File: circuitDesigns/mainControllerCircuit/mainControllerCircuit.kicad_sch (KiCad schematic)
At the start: 49 parts, among them J1 USB_A, J2 USB_A, J3 USB_A, J4 Conn_01x15_Pin, J5 Conn_01x15_Pin, J6 Conn_01x16_Socket, J7 OutputVCC, Q1 AO3400A, Q10 AO3400A, Q11 AO3400A, Q12 AO3400A, Q13 AO3400A, Q14 AO3400A, Q15 AO3400A, Q16 AO3400A, Q2 AO3400A, Q3 AO3400A, Q4 AO3400A, Q5 AO3400A, Q6 AO3400A, Q7 AO3400A, Q8 AO3400A, Q9 AO3400A

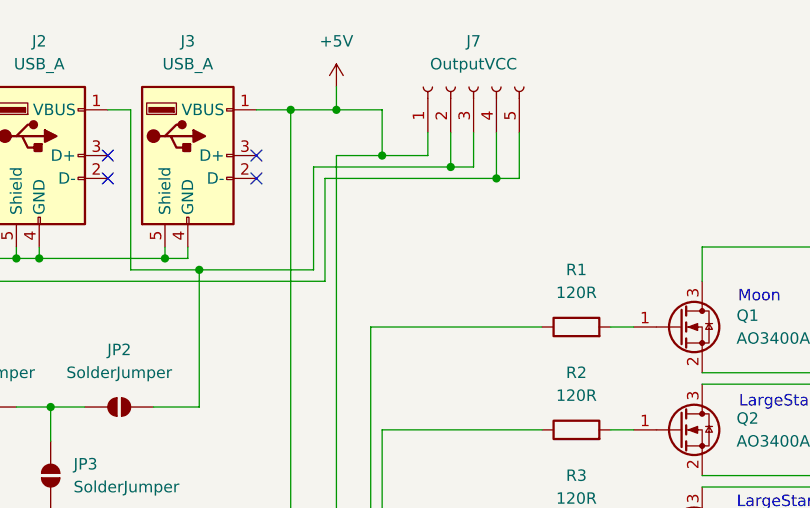
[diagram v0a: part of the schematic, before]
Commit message: Updates design files for main controller to better accomodate to manufacturer specs
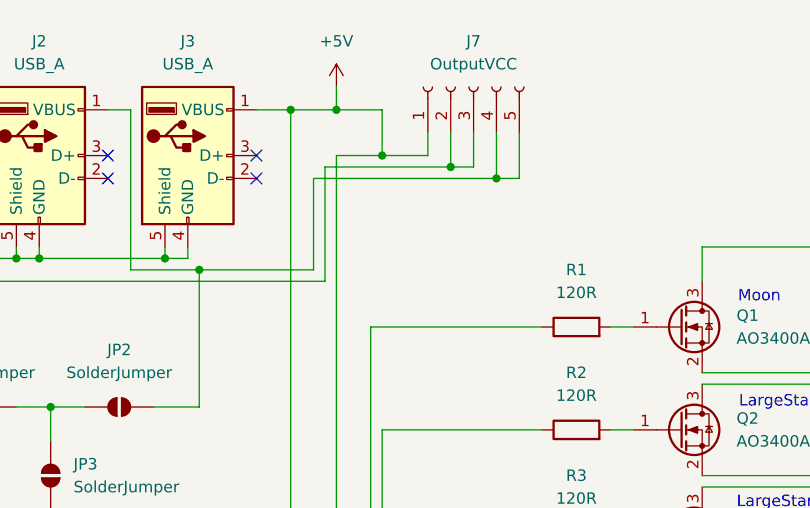
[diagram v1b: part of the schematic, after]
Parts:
- R18: footprint Resistor_SMD:R_1206_3216Metric_Pad1.30x1.75mm_HandSolder -> Resistor_THT:R_Axial_DIN0207_L6.3mm_D2.5mm_P7.62mm_Horizontal
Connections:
- net at J2.1 (VBUS), JP2.2 (B): now also J7.4 (Pin_4), J7.5 (Pin_5); no longer J7.2 (Pin_2), J7.3 (Pin_3)
- net at J1.1 (VBUS), JP1.2 (B): now also J7.2 (Pin_2), J7.3 (Pin_3); no longer J7.4 (Pin_4), J7.5 (Pin_5)
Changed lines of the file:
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@@
+	)
+	(junction
+		(at 123.19 26.67)
+		(diameter 0)
+		(color 0 0 0 0)
+	)
+	(junction
+		(at 173.99 109.22)
+		(diameter 0)
+		(color 0 0 0 0)
+	)
+	(junction
+		(at 78.74 40.64)
+		(diameter 0)
+		(color 0 0 0 0)
+	)
+	(junction
+		(at 260.35 38.1)
+		(diameter 0)
+		(color 0 0 0 0)
+	)
+	(junction
+		(at 245.11 27.94)
+		(diameter 0)
+		(color 0 0 0 0)
+	)
+	(junction
+		(at 82.55 38.1)
+		(diameter 0)
+		(color 0 0 0 0)
+	)
+	(junction
+		(at 265.43 44.45)
+		(diameter 0)
+		(color 0 0 0 0)
+	)
+	(junction
+		(at 262.89 39.37)
+		(diameter 0)
+		(color 0 0 0 0)
+	)
+	(junction
+		(at 278.13 30.48)
+		(diameter 0)
+		(color 0 0 0 0)
+	)
+	(junction
+		(at 252.73 34.29)
+		(diameter 0)
+		(color 0 0 0 0)
+	)
+	(junction
+		(at 267.97 45.72)
+		(diameter 0)
+		(color 0 0 0 0)
+	)
+	(junction
+		(at 173.99 62.23)
+		(diameter 0)
+		(color 0 0 0 0)
+	)
+	(junction
+		(at 173.99 132.08)
+		(diameter 0)
+		(color 0 0 0 0)
+	)
+	(junction
+		(at 173.99 73.66)
+		(diameter 0)
+		(color 0 0 0 0)
+	)
+	(junction
+		(at 270.51 40.64)
+		(diameter 0)
+		(color 0 0 0 0)
+	)
+	(junction
+		(at 273.05 41.91)
+		(diameter 0)
+		(color 0 0 0 0)
+	)
+	(junction
+		(at 173.99 97.79)
+		(diameter 0)
+		(color 0 0 0 0)
+	)
+	(junction
+		(at 234.95 62.23)
+		(diameter 0)
+		(color 0 0 0 0)
+	)
+	(junction
+		(at 135.89 29.21)
+		(diameter 0)
+		(color 0 0 0 0)
+	)
+	(junction
+		(at 250.19 33.02)
+		(diameter 0)
+		(color 0 0 0 0)
+	)
+	(junction
+		(at 234.95 96.52)
+		(diameter 0)
+		(color 0 0 0 0)
+	)
+	(junction
+		(at 280.67 29.21)
+		(diameter 0)
+		(color 0 0 0 0)
+	)
+	(junction
+		(at 85.09 38.1)
+		(diameter 0)
+		(color 0 0 0 0)
+	)
+	(junction
+		(at 173.99 146.05)
+		(diameter 0)
+		(color 0 0 0 0)
+	)
+	(junction
+		(at 275.59 43.18)
+		(diameter 0)
+		(color 0 0 0 0)
 	)
 	(junction
 		(at 130.81 27.94)
-		(diameter 0)
-		(color 0 0 0 0)
-	)
-	(junction
-		(at 123.19 26.67)
-		(diameter 0)
-		(color 0 0 0 0)
-	)
-	(junction
-		(at 173.99 109.22)
-		(diameter 0)
-		(color 0 0 0 0)
-	)
-	(junction
-		(at 78.74 40.64)
-		(diameter 0)
-		(color 0 0 0 0)
-	)
-	(junction
-		(at 260.35 38.1)
-		(diameter 0)
-		(color 0 0 0 0)
-	)
-	(junction
-		(at 135.89 29.21)
-		(diameter 0)
-		(color 0 0 0 0)
-	)
-	(junction
-		(at 245.11 27.94)
-		(diameter 0)
-		(color 0 0 0 0)
-	)
-	(junction
-		(at 82.55 38.1)
-		(diameter 0)
-		(color 0 0 0 0)
-	)
-	(junction
-		(at 265.43 44.45)
-		(diameter 0)
-		(color 0 0 0 0)
-	)
-	(junction
-		(at 262.89 39.37)
-		(diameter 0)
-		(color 0 0 0 0)
-	)
-	(junction
-		(at 278.13 30.48)
-		(diameter 0)
-		(color 0 0 0 0)
-	)
-	(junction
-		(at 252.73 34.29)
-		(diameter 0)
-		(color 0 0 0 0)
-	)
-	(junction
-		(at 267.97 45.72)
-		(diameter 0)
-		(color 0 0 0 0)
-	)
-	(junction
-		(at 173.99 62.23)
-		(diameter 0)
-		(color 0 0 0 0)
-	)
-	(junction
-		(at 173.99 132.08)
-		(diameter 0)
-		(color 0 0 0 0)
-	)
-	(junction
-		(at 173.99 73.66)
-		(diameter 0)
-		(color 0 0 0 0)
-	)
-	(junction
-		(at 270.51 40.64)
-		(diameter 0)
-		(color 0 0 0 0)
-	)
-	(junction
-		(at 273.05 41.91)
-		(diameter 0)
-		(color 0 0 0 0)
-	)
-	(junction
-		(at 173.99 97.79)
-		(diameter 0)
-		(color 0 0 0 0)
-	)
-	(junction
-		(at 234.95 62.23)
-		(diameter 0)
-		(color 0 0 0 0)
-	)
-	(junction
-		(at 250.19 33.02)
-		(diameter 0)
-		(color 0 0 0 0)
-	)
-	(junction
-		(at 234.95 96.52)
-		(diameter 0)
-		(color 0 0 0 0)
-	)
-	(junction
-		(at 280.67 29.21)
-		(diameter 0)
-		(color 0 0 0 0)
-	)
-	(junction
-		(at 85.09 38.1)
-		(diameter 0)
-		(color 0 0 0 0)
-	)
-	(junction
-		(at 173.99 146.05)
-		(diameter 0)
-		(color 0 0 0 0)
-	)
-	(junction
-		(at 275.59 43.18)
 		(diameter 0)
 		(color 0 0 0 0)
@@
 	(wire
 		(pts
-			(xy 116.84 29.21) (xy 116.84 40.64)
-		)
-		(stroke
-			(width 0)
-			(type default)
-		)
-	)
-	(wire
-		(pts
 			(xy 148.59 92.71) (xy 151.13 92.71)
 		)
@@
 	(wire
 		(pts
-			(xy 130.81 27.94) (xy 115.57 27.94)
-		)
-		(stroke
-			(width 0)
-			(type default)
-		)
-	)
-	(wire
-		(pts
 			(xy 148.59 80.01) (xy 151.13 80.01)
 		)
@@
 	(wire
 		(pts
-			(xy 135.89 29.21) (xy 116.84 29.21)
-		)
-		(stroke
-			(width 0)
-			(type default)
-		)
-	)
-	(wire
-		(pts
 			(xy 113.03 21.59) (xy 118.11 21.59)
 		)
@@
 	(wire
 		(pts
+			(xy 115.57 29.21) (xy 135.89 29.21)
+		)
+		(stroke
+			(width 0)
+			(type default)
+		)
+	)
+	(wire
+		(pts
 			(xy 219.71 74.93) (xy 238.76 74.93)
 		)
@@
 	(wire
 		(pts
+			(xy 116.84 27.94) (xy 130.81 27.94)
+		)
+		(stroke
+			(width 0)
+			(type default)
+		)
+	)
+	(wire
+		(pts
 			(xy 180.34 33.02) (xy 250.19 33.02)
 		)
@@
 	(wire
 		(pts
+			(xy 116.84 27.94) (xy 116.84 40.64)
+		)
+		(stroke
+			(width 0)
+			(type default)
+		)
+	)
+	(wire
+		(pts
 			(xy 26.67 135.89) (xy 26.67 143.51)
 		)
@@
 	(wire
 		(pts
-			(xy 115.57 27.94) (xy 115.57 39.37)
-		)
-		(stroke
-			(width 0)
-			(type default)
-		)
-	)
-	(wire
-		(pts
 			(xy 99.06 38.1) (xy 99.06 36.83)
 		)
@@
 		(pts
 			(xy 209.55 125.73) (xy 212.09 125.73)
+		)
+		(stroke
+			(width 0)
+			(type default)
+		)
+	)
+	(wire
+		(pts
+			(xy 115.57 29.21) (xy 115.57 39.37)
 		)
 		(stroke
@@
 			)
 		)
-		(property "Footprint" "Resistor_SMD:R_1206_3216Metric_Pad1.30x1.75mm_HandSolder"
+		(property "Footprint" "Resistor_THT:R_Axial_DIN0207_L6.3mm_D2.5mm_P7.62mm_Horizontal"
 			(at 28.448 132.08 90)
 			(effects

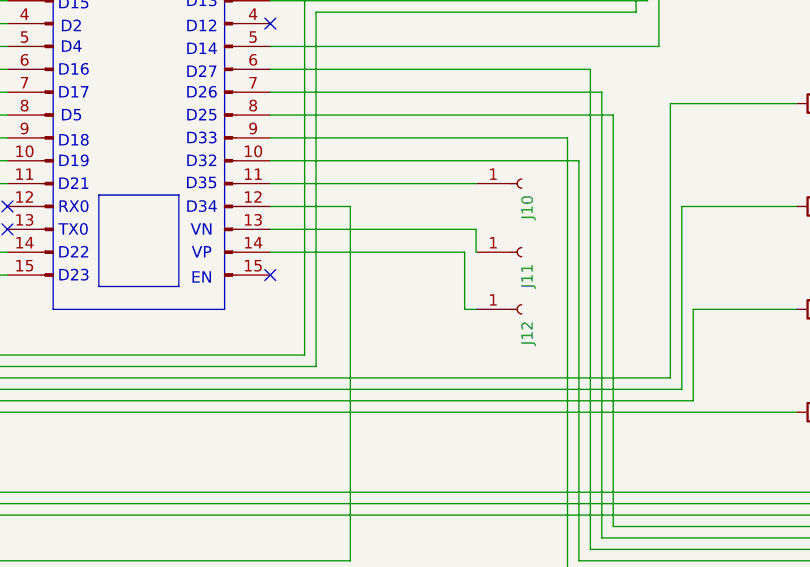
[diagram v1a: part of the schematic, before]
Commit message: Increases clearances between the pads to not have a safer margin above the minimum limits of the manufacturer
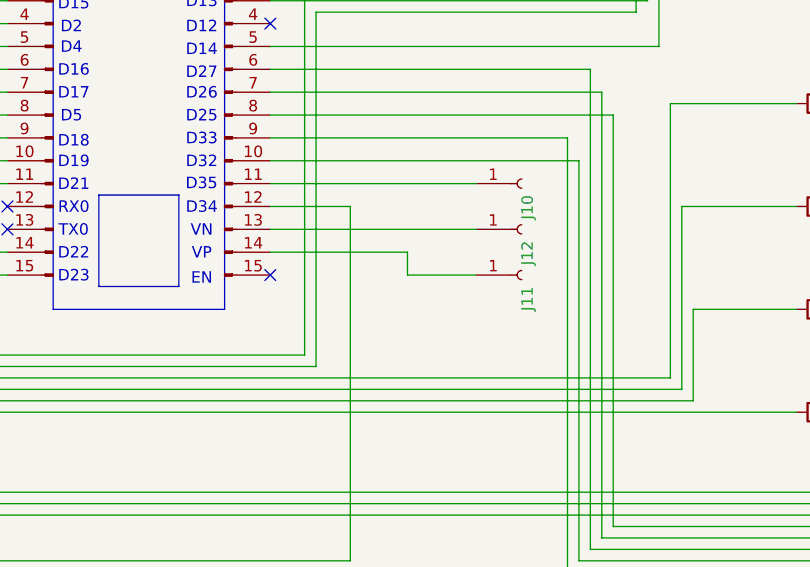
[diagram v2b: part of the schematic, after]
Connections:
- net at J11.1 (Pin_1): now also J5.14 (Pin_14); no longer J5.13 (Pin_13)
- net at J12.1 (Pin_1): now also J5.13 (Pin_13); no longer J5.14 (Pin_14)
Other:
- moved on the sheet: J11, J12
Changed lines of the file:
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@@
 	(wire
 		(pts
-			(xy 105.41 115.57) (xy 104.14 115.57)
-		)
-		(stroke
-			(width 0)
-			(type default)
-		)
-	)
-	(wire
-		(pts
 			(xy 53.34 101.6) (xy 43.18 101.6)
 		)
@@
 	(wire
 		(pts
-			(xy 104.14 115.57) (xy 104.14 109.22)
+			(xy 120.65 93.98) (xy 82.55 93.98)
 		)
 		(stroke
@@
 	(wire
 		(pts
-			(xy 120.65 93.98) (xy 82.55 93.98)
+			(xy 118.11 142.24) (xy 194.31 142.24)
 		)
 		(stroke
@@
 	(wire
 		(pts
-			(xy 118.11 142.24) (xy 194.31 142.24)
+			(xy 173.99 151.13) (xy 173.99 146.05)
 		)
 		(stroke
@@
 	(wire
 		(pts
-			(xy 173.99 151.13) (xy 173.99 146.05)
+			(xy 243.84 45.72) (xy 267.97 45.72)
 		)
 		(stroke
@@
 	(wire
 		(pts
-			(xy 243.84 45.72) (xy 267.97 45.72)
+			(xy 82.55 109.22) (xy 97.79 109.22)
 		)
 		(stroke
@@
 	(wire
 		(pts
+			(xy 97.79 109.22) (xy 97.79 111.76)
+		)
+		(stroke
+			(width 0)
+			(type default)
+		)
+	)
+	(wire
+		(pts
 			(xy 250.19 22.86) (xy 250.19 33.02)
 		)
@@
 	(wire
 		(pts
-			(xy 104.14 109.22) (xy 82.55 109.22)
-		)
-		(stroke
-			(width 0)
-			(type default)
-		)
-	)
-	(wire
-		(pts
 			(xy 130.81 24.13) (xy 130.81 27.94)
 		)
@@
 	(wire
 		(pts
+			(xy 82.55 106.68) (xy 105.41 106.68)
+		)
+		(stroke
+			(width 0)
+			(type default)
+		)
+	)
+	(wire
+		(pts
 			(xy 140.97 115.57) (xy 129.54 115.57)
 		)
@@
 	(wire
 		(pts
+			(xy 97.79 111.76) (xy 105.41 111.76)
+		)
+		(stroke
+			(width 0)
+			(type default)
+		)
+	)
+	(wire
+		(pts
 			(xy 82.55 54.61) (xy 86.36 54.61)
 		)
@@
 	(wire
 		(pts
-			(xy 105.41 109.22) (xy 105.41 106.68)
-		)
-		(stroke
-			(width 0)
-			(type default)
-		)
-	)
-	(wire
-		(pts
 			(xy 26.67 124.46) (xy 26.67 128.27)
 		)
@@
 	(wire
 		(pts
-			(xy 105.41 106.68) (xy 82.55 106.68)
-		)
-		(stroke
-			(width 0)
-			(type default)
-		)
-	)
-	(wire
-		(pts
 			(xy 182.88 35.56) (xy 255.27 35.56)
 		)
@@
 	(symbol
 		(lib_id "Connector:Conn_01x01_Socket")
-		(at 110.49 109.22 0)
+		(at 110.49 111.76 0)
 		(unit 1)
 		(exclude_from_sim no)
@@
 		(dnp no)
 		(property "Reference" "J11"
-			(at 111.1251 110.49 90)
+			(at 111.1251 113.03 90)
 			(effects
 				(font
@@
 		)
 		(property "Value" "~"
-			(at 108.5851 110.49 90)
+			(at 108.5851 113.03 90)
 			(effects
 				(font
@@
 		)
 		(property "Footprint" "Connector_PinSocket_2.54mm:PinSocket_1x01_P2.54mm_Vertical"
-			(at 110.49 109.22 0)
+			(at 110.49 111.76 0)
 			(effects
 				(font
@@
 		)
 		(property "Datasheet" "~"
-			(at 110.49 109.22 0)
+			(at 110.49 111.76 0)
 			(effects
 				(font
@@
 		)
 		(property "Description" "Generic connector, single row, 01x01, script generated"
-			(at 110.49 109.22 0)
+			(at 110.49 111.76 0)
 			(effects
 				(font
@@
 	(symbol
 		(lib_id "Connector:Conn_01x01_Socket")
-		(at 110.49 115.57 0)
+		(at 110.49 106.68 0)
 		(unit 1)
 		(exclude_from_sim no)
@@
 		(dnp no)
 		(property "Reference" "J12"
-			(at 111.1251 116.84 90)
+			(at 111.1251 107.95 90)
 			(effects
 				(font
@@
 		)
 		(property "Value" "~"
-			(at 108.5851 116.84 90)
+			(at 108.5851 107.95 90)
 			(effects
 				(font
@@
 		)
 		(property "Footprint" "Connector_PinSocket_2.54mm:PinSocket_1x01_P2.54mm_Vertical"
-			(at 110.49 115.57 0)
+			(at 110.49 106.68 0)
 			(effects
 				(font
@@
 		)
 		(property "Datasheet" "~"
-			(at 110.49 115.57 0)
+			(at 110.49 106.68 0)
 			(effects
 				(font
@@
 		)
 		(property "Description" "Generic connector, single row, 01x01, script generated"
-			(at 110.49 115.57 0)
+			(at 110.49 106.68 0)
 			(effects
 				(font

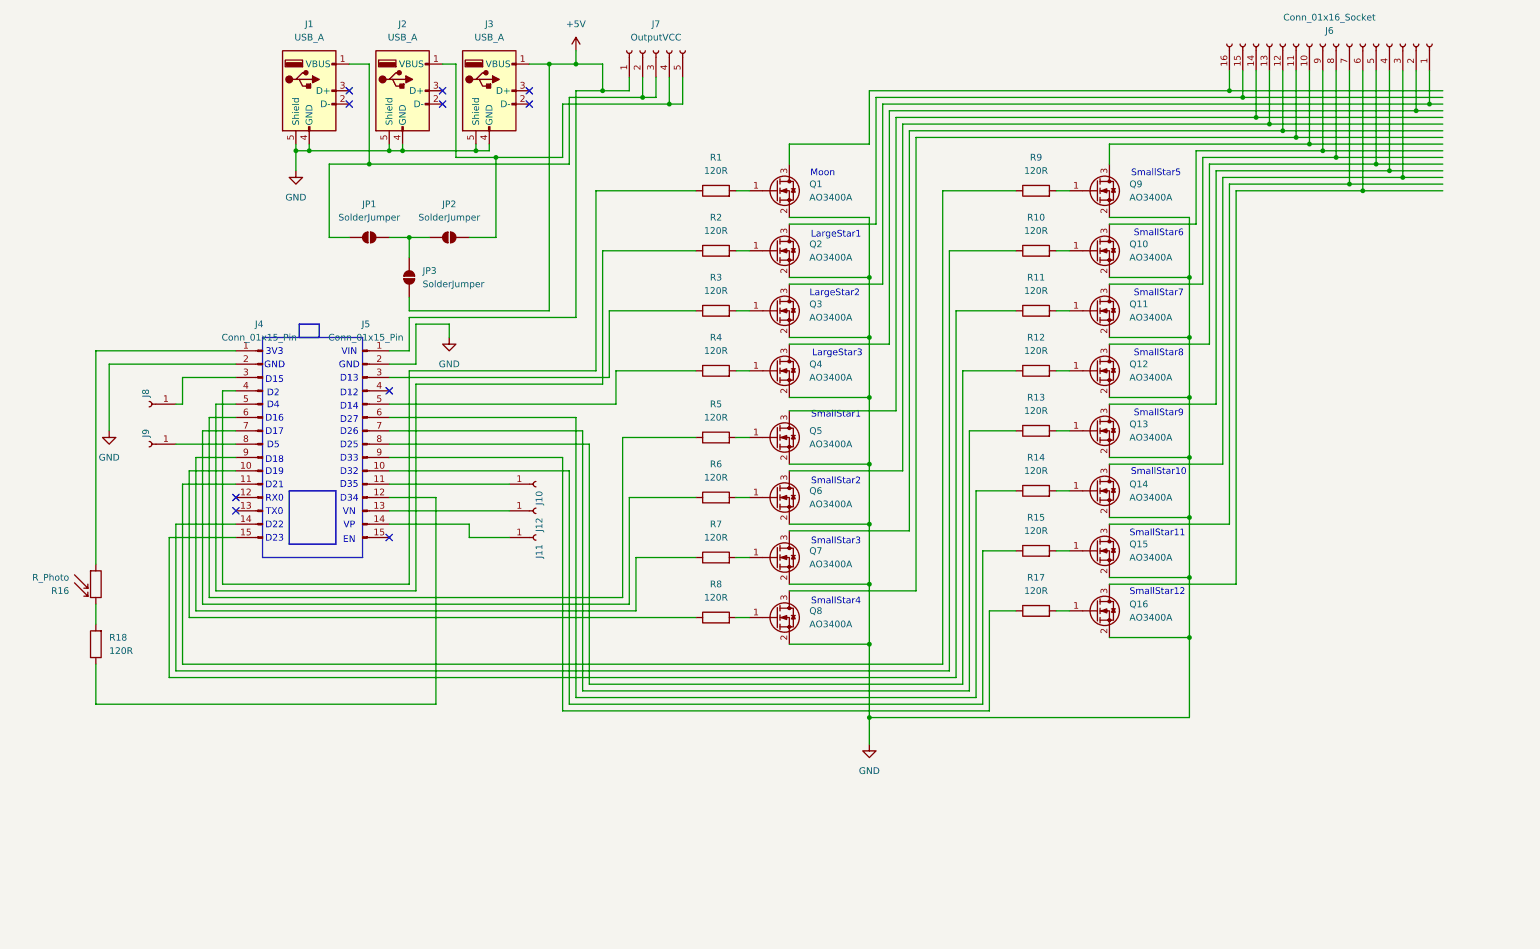
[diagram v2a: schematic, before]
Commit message: Fixes error in controller circuit: mosfets were missing pull down resistor
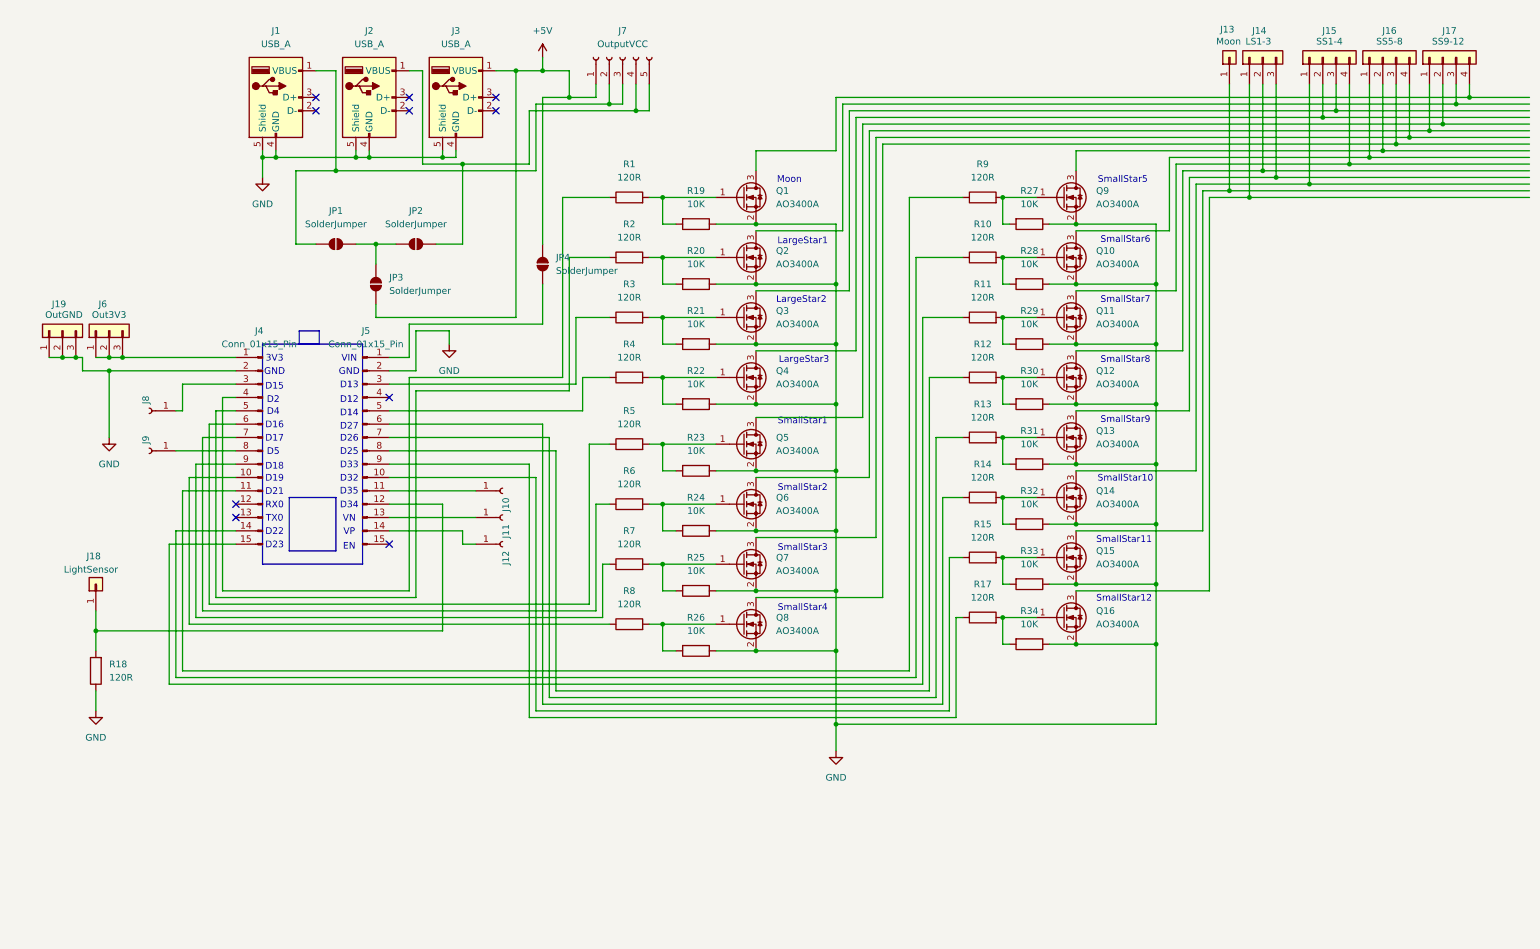
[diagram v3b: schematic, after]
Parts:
- removed J6: Conn_01x16_Socket, Connector_PinSocket_2.54mm:PinSocket_1x16_P2.54mm_Vertical, symbol Connector:Conn_01x16_Socket
- removed R16: R_Photo, Connector_PinSocket_2.54mm:PinSocket_1x02_P2.54mm_Vertical, symbol Device:R_Photo
- added J13: Moon, Connector_PinSocket_2.54mm:PinSocket_1x01_P2.54mm_Vertical, symbol Connector_Generic:Conn_01x01
- added J14: LS1-3, Connector_PinSocket_2.54mm:PinSocket_1x03_P2.54mm_Vertical, symbol Connector_Generic:Conn_01x03
- added J15: SS1-4, Connector_PinSocket_2.54mm:PinSocket_1x04_P2.54mm_Vertical, symbol Connector_Generic:Conn_01x04
- added J16: SS5-8, Connector_PinSocket_2.54mm:PinSocket_1x04_P2.54mm_Vertical, symbol Connector_Generic:Conn_01x04
- added J17: SS9-12, Connector_PinSocket_2.54mm:PinSocket_1x04_P2.54mm_Vertical, symbol Connector_Generic:Conn_01x04
- added J18: LightSensor, Connector_PinSocket_2.54mm:PinSocket_1x01_P2.54mm_Vertical, symbol Connector_Generic:Conn_01x01
- added J19: OutGND, Connector_PinSocket_2.54mm:PinSocket_1x03_P2.54mm_Vertical, symbol Connector_Generic:Conn_01x03
- added J6: Out3V3, Connector_PinSocket_2.54mm:PinSocket_1x03_P2.54mm_Vertical, symbol Connector_Generic:Conn_01x03
- added JP4: SolderJumper, Connector_PinSocket_2.54mm:PinSocket_1x02_P2.54mm_Vertical, symbol Jumper:SolderJumper_2_Open
- added R19, R20, R21, R22, R23, R24, R25, R26, R27, R28, R29, R30, R31, R32, R33, R34: 10K, Resistor_THT:R_Axial_DIN0207_L6.3mm_D2.5mm_P7.62mm_Horizontal, symbol Device:R
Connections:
- net +5V: now also JP4.2 (B); no longer J5.1 (Pin_1)
- net GND: now also R18.1, J19.1 (Pin_1), J19.2 (Pin_2), J19.3 (Pin_3), R19.1, R20.1, R21.1, R22.1, R23.1, R24.1, R25.1, R26.1, R27.1, R28.1, R29.1, R30.1, R31.1, R32.1, R33.1, R34.1
- net at Q1.1 (G), R1.2: now also R19.2
- net at Q11.1 (G), R11.2: now also R29.2
- net at Q11.3 (D): now also J15.4 (Pin_4)
- net at J4.1 (Pin_1): now also J6.1 (Pin_1), J6.2 (Pin_2), J6.3 (Pin_3)
- net at R18.2: now also J5.12 (Pin_12), J18.1 (Pin_1)
- net at Q2.1 (G), R2.2: now also R20.2
- net at Q13.1 (G), R13.2: now also R31.2
- net at Q13.3 (D): now also J14.3 (Pin_3)
- net at Q3.3 (D): now also J15.3 (Pin_3)
- net at Q9.3 (D): now also J16.2 (Pin_2)
- net at Q8.3 (D): now also J16.3 (Pin_3)
- net at Q7.3 (D): now also J16.4 (Pin_4)
- net at Q6.3 (D): now also J17.1 (Pin_1)
- net at Q5.3 (D): now also J17.2 (Pin_2)
- net at Q2.3 (D): now also J17.3 (Pin_3)
- net at Q1.3 (D): now also J17.4 (Pin_4)
- net at Q4.3 (D): now also J15.2 (Pin_2)
- net at Q14.3 (D): now also J15.1 (Pin_1)
- net at Q12.3 (D): now also J14.2 (Pin_2)
- net at Q16.3 (D): now also J14.1 (Pin_1)
- net at Q15.3 (D): now also J13.1 (Pin_1)
- net at Q10.3 (D): now also J16.1 (Pin_1)
- net at Q7.1 (G), R7.2: now also R25.2
- net at Q4.1 (G), R4.2: now also R22.2
- net at Q14.1 (G), R14.2: now also R32.2
- net at Q12.1 (G), R12.2: now also R30.2
- net at Q5.1 (G), R5.2: now also R23.2
- net at Q9.1 (G), R9.2: now also R27.2
- net at Q10.1 (G), R10.2: now also R28.2
- net at Q6.1 (G), R6.2: now also R24.2
- net at Q8.1 (G), R8.2: now also R26.2
- net at J11.1 (Pin_1): now also J5.13 (Pin_13); no longer J5.14 (Pin_14)
- net at Q15.1 (G), R15.2: now also R33.2
- net at Q3.1 (G), R3.2: now also R21.2
- net at J12.1 (Pin_1): now also J5.14 (Pin_14); no longer J5.13 (Pin_13)
- net at Q16.1 (G), R17.2: now also R34.2
- new net: J5.1 (Pin_1), JP4.1 (A)
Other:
- moved on the sheet: J1, J10, J11, J12, J2, J3, J4, J5, J7, J8, J9, JP1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
